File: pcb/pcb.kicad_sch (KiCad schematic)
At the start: 20 parts, among them J1 Conn_01x04_MountingPin, J2 Conn_01x04_MountingPin, J4 Conn_ARM_SWD_TagConnect_TC203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, U1 THVD1451, U2 STM32G0B1KBUx, U3 AP2210

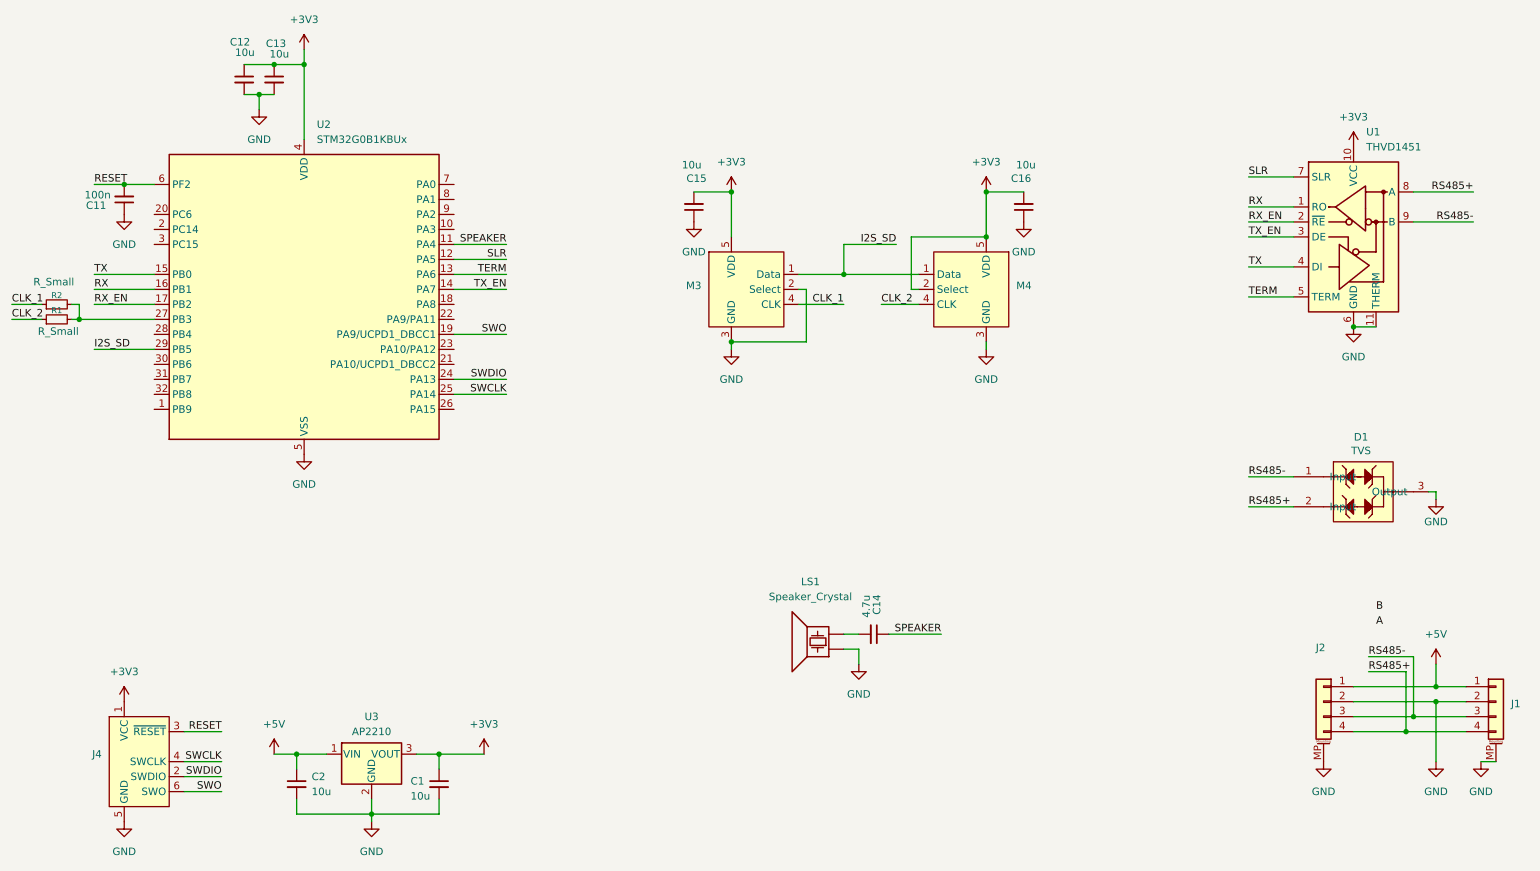
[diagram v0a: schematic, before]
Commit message: rs485 re route
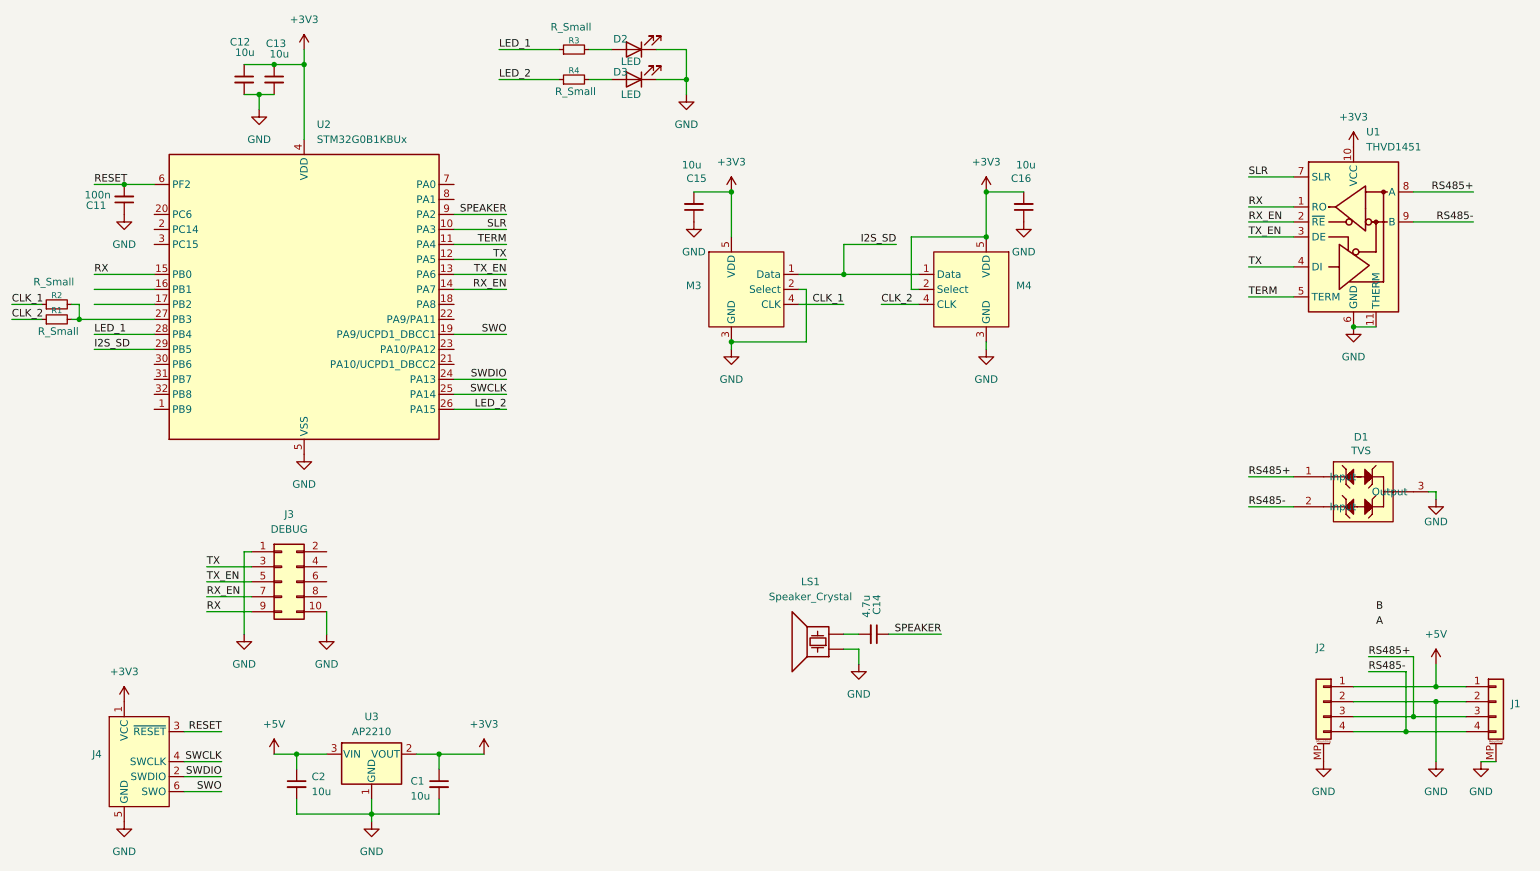
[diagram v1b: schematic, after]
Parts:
- added D2, D3: LED, Diode_SMD:D_0402_1005Metric, symbol Device:LED
- added J3: DEBUG, PinHeader_2x05_P1.27mm_Vertical_SMD, symbol Connector_Generic:Conn_02x05_Odd_Even
- added R3, R4: R_Small, Resistor_SMD:R_0402_1005Metric, symbol Device:R_Small
- LS1: footprint goatworks-footprint-library:OWR-061220LA-32 -> goatworks-footprint-library:PKMCS0909E4000-R1
- U1: footprint Package_SON:VSON-10-1EP_3x3mm_P0.5mm_EP1.65x2.4mm -> Package_SON:VSON-10-1EP_3x3mm_P0.5mm_EP1.65x2.4mm_ThermalVias
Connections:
- net +3V3: now also U3.2 (VOUT); no longer U3.3 (VOUT)
- net +5V: now also U3.3 (VIN); no longer U3.1 (VIN)
- net GND: now also U3.1 (GND), D2.1 (K), D3.1 (K), J3.1 (Pin_1), J3.10 (Pin_10); no longer U3.2 (GND)
- net RS485+: now also D1.1 (Input), J1.3 (Pin_3), J2.3 (Pin_3); no longer D1.2 (Input), J1.4 (Pin_4), J2.4 (Pin_4)
- net RS485-: now also D1.2 (Input), J1.4 (Pin_4), J2.4 (Pin_4); no longer D1.1 (Input), J1.3 (Pin_3), J2.3 (Pin_3)
- net RX: now also U2.15 (PB0), J3.9 (Pin_9); no longer U2.16 (PB1)
- net RX_EN: now also U2.14 (PA7), J3.7 (Pin_7); no longer U2.17 (PB2)
- net SLR: now also U2.10 (PA3); no longer U2.12 (PA5)
- net SPEAKER: now also U2.9 (PA2); no longer U2.11 (PA4)
- net TERM: now also U2.11 (PA4); no longer U2.13 (PA6)
- net TX: now also U2.12 (PA5), J3.3 (Pin_3); no longer U2.15 (PB0)
- net TX_EN: now also U2.13 (PA6), J3.5 (Pin_5); no longer U2.14 (PA7)
- net LED_2: now reaches U2.26 (PA15)
- net LED_2: now also R4.1
- net LED_1: now reaches U2.28 (PB4)
- net LED_1: now also R3.1
- new net: D2.2 (A), R3.2
- new net: D3.2 (A), R4.2

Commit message: small tweaks
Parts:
- added C3: 10u, Capacitor_SMD:C_0402_1005Metric, symbol Device:C_Small
- added TP1: CLK, goatworks-footprint-library:tp-ev24, symbol Connector:TestPoint_Small
- added TP2, TP7, TP8: GND, goatworks-footprint-library:tp-ev24, symbol Connector:TestPoint_Small
- added TP4: SD, goatworks-footprint-library:tp-ev24, symbol Connector:TestPoint_Small
- added TP5: 5V, goatworks-footprint-library:tp-ev24, symbol Connector:TestPoint_Small
- added TP6: 3V3, goatworks-footprint-library:tp-ev24, symbol Connector:TestPoint_Small
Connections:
- net +3V3: now also C3.1, TP6.1
- net +5V: now also TP5.1
- net GND: now also C3.2, TP2.1, TP7.1, TP8.1
- net I2S_SD: now also TP4.1
- net at R1.2, R2.2, U2.27 (PB3): now also TP1.1
